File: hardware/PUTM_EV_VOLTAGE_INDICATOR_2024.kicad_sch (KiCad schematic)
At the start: 10 parts, among them J1 WIRE, J2 WIRE, J3 SCREW_TERMINAL, J4 SCREW_TERMINAL, J5 SCREW_TERMINAL, J6 SCREW_TERMINAL, J7 WIRE, J8 WIRE

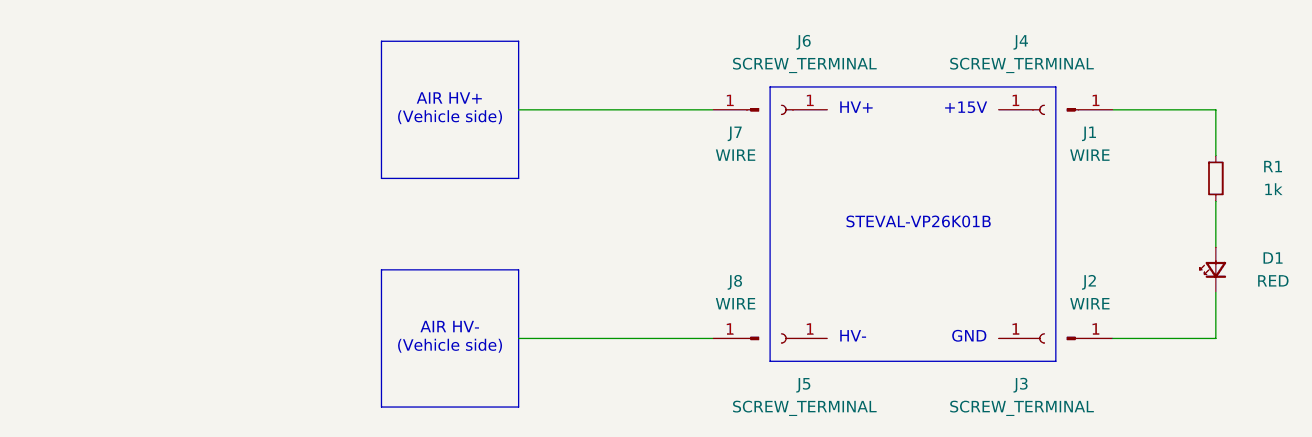
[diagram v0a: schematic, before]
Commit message: plan b using a diac relaxation oscilator
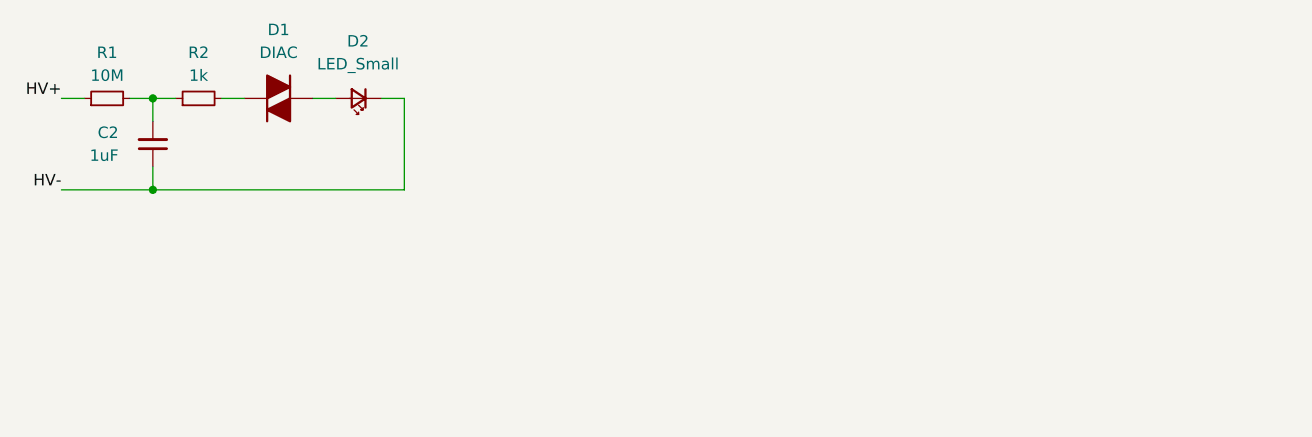
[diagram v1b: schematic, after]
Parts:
- removed D1: RED, symbol Device:LED_Small
- removed J1, J2, J7, J8: WIRE, symbol Connector:Conn_01x01_Pin
- removed J3, J4, J5, J6: SCREW_TERMINAL, symbol Connector:Conn_01x01_Socket
- added C2: 1uF, symbol Device:C_Small
- added D1: DIAC, symbol Device:DIAC
- added D2: LED_Small, symbol Device:LED_Small
- added R2: 1k, symbol Device:R_Small
- R1: value 1k -> 10M
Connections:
- net HV+: now reaches R1.1
- net at R1.2: now also C2.2, R2.1
- new net: D1.1 (K), R2.2
- new net: D1.2 (A), D2.2 (A)
- new net HV-: C2.1, D2.1 (K)
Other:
- note removed: "+15V"
- note removed: "AIR HV+ (Vehicle side)"
- note removed: "AIR HV- (Vehicle side)"
- note removed: "GND"
- note removed: "HV+"
- note removed: "HV-"
- note removed: "STEVAL-VP26K01B"
